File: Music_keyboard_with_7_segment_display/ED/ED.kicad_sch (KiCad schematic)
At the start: 1 part

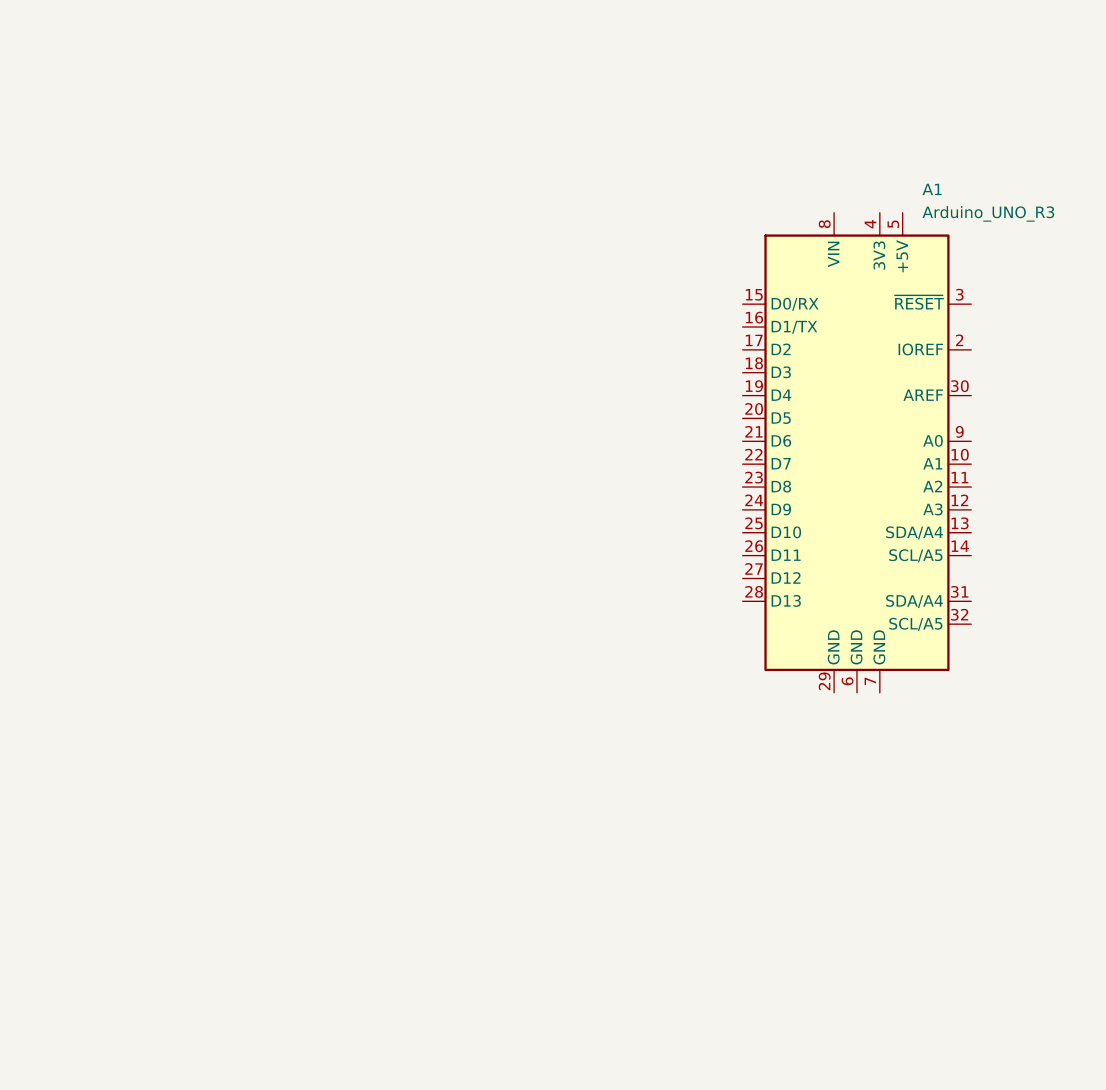
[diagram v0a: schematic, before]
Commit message: ED definition
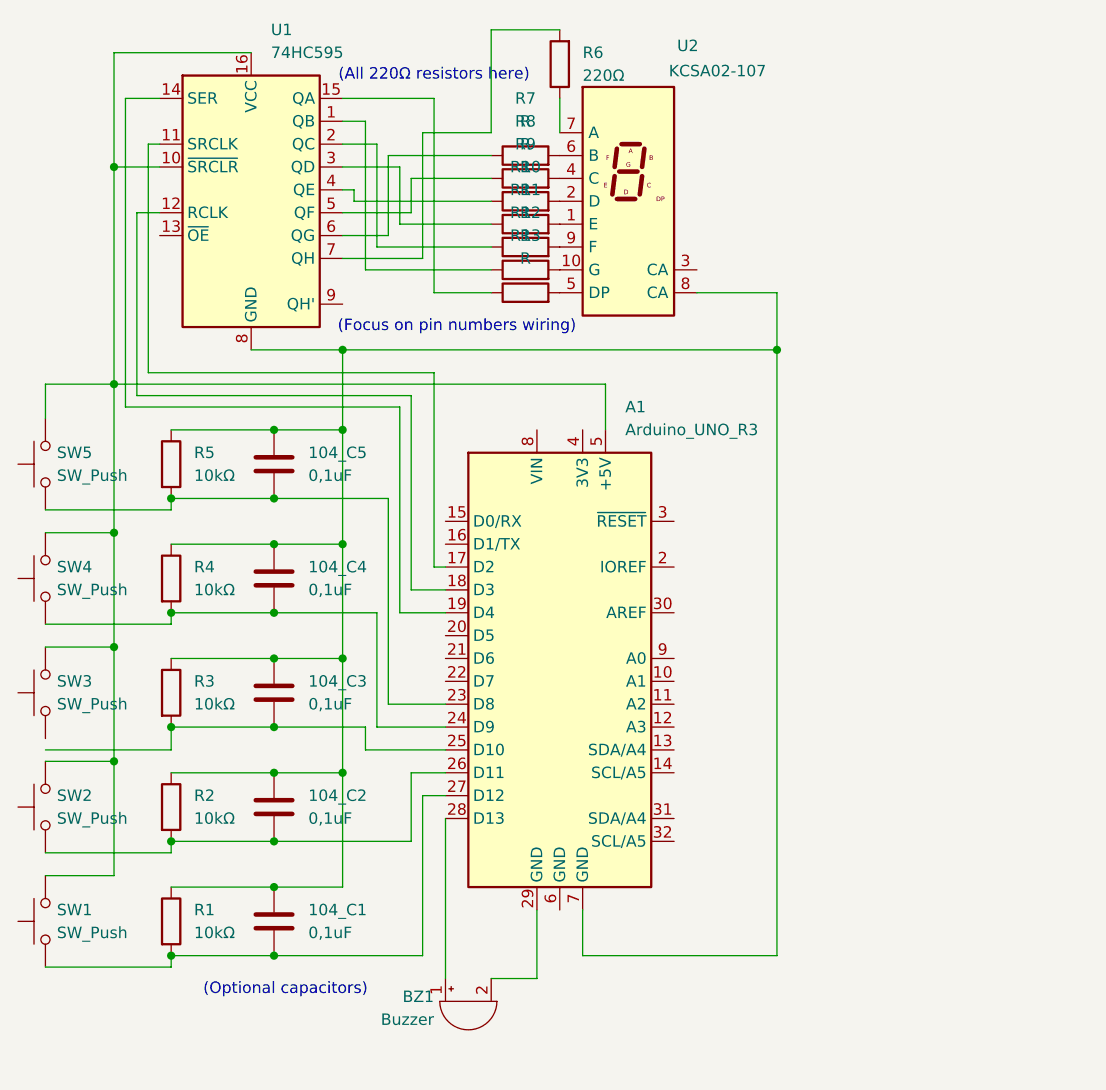
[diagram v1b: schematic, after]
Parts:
- added 104_C1, 104_C2, 104_C3, 104_C4, 104_C5: 0,1uF, symbol Device:C
- added BZ1: Buzzer, symbol Device:Buzzer
- added R1, R2, R3, R4, R5: 10kΩ, symbol Device:R
- added R10, R11, R12, R13, R7, R8, R9: R, symbol Device:R
- added R6: 220Ω, symbol Device:R
- added SW1, SW2, SW3, SW4, SW5: SW_Push, symbol Switch:SW_Push
- added U1: 74HC595, symbol 74xx:74HC595
- added U2: KCSA02-107, Display_7Segment:KCSC02-107, symbol Display_Character:KCSA02-107
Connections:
- net at A1.17 (D2): now also U1.11 (SRCLK)
- net at A1.18 (D3): now also U1.12 (RCLK)
- net at A1.19 (D4): now also U1.14 (SER)
- net at A1.23 (D8): now also 104_C5.2, R5.2, SW5.1
- net at A1.24 (D9): now also 104_C4.2, R4.2, SW4.1
- net at A1.25 (D10): now also 104_C3.2, R3.2
- net at A1.26 (D11): now also 104_C2.2, R2.2, SW2.1
- net at A1.27 (D12): now also 104_C1.2, R1.2, SW1.1
- net at A1.28 (D13): now also BZ1.1 (+)
- net at A1.29 (GND): now also BZ1.2 (-)
- net at A1.5 (+5V): now also SW1.2, SW2.2, SW3.2, SW4.2, SW5.2, U1.10 (~{SRCLR}), U1.16 (VCC)
- net at A1.7 (GND): now also 104_C1.1, 104_C2.1, 104_C3.1, 104_C4.1, 104_C5.1, R1.1, R2.1, R3.1, R4.1, R5.1, U1.8 (GND), U2.8 (CA)
- new net: R10.1, U1.3 (QD)
- new net: R10.2, U2.1 (E)
- new net: R8.1, U1.5 (QF)
- new net: R8.2, U2.4 (C)
- new net: R12.1, U1.1 (QB)
- new net: R13.1, U1.15 (QA)
- new net: R11.1, U1.2 (QC)
- new net: R9.1, U1.4 (QE)
- new net: R7.1, U1.6 (QG)
- new net: R6.2, U1.7 (QH)
- new net: R13.2, U2.5 (DP)
- new net: R12.2, U2.10 (G)
- new net: R9.2, U2.2 (D)
- new net: R7.2, U2.6 (B)
- new net: R6.1, U2.7 (A)
- new net: R11.2, U2.9 (F)
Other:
- note added: "(All 220Ω resistors here)"
- note added: "(Focus on pin numbers wiring)"
- note added: "(Optional capacitors)"
- moved on the sheet: A1

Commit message: GuitarNeck
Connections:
- net at 104_C3.2, A1.25 (D10), R3.2: now also SW3.1
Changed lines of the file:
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@@
 	(wire
 		(pts
-			(xy 104.14 118.11) (xy 118.11 118.11)
+			(xy 104.14 116.84) (xy 118.11 116.84)
 		)
 		(stroke
@@
 	(wire
 		(pts
-			(xy 118.11 115.57) (xy 118.11 118.11)
-		)
-		(stroke
+			(xy 118.11 115.57) (xy 118.11 116.84)
+		)
+		(stroke

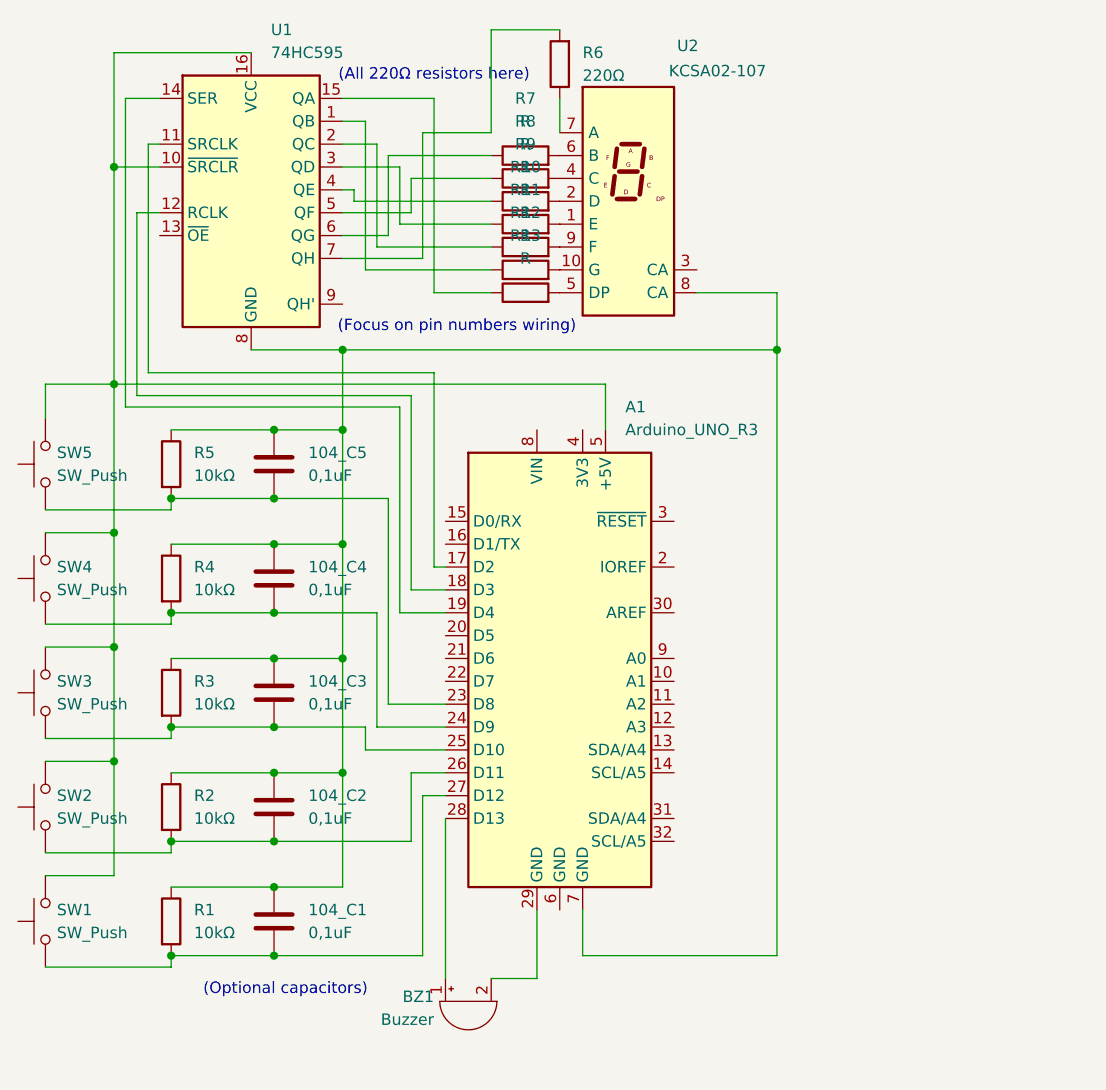
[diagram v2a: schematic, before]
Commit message: Capacitors before buttons and buzzer connected to pwm pin 6
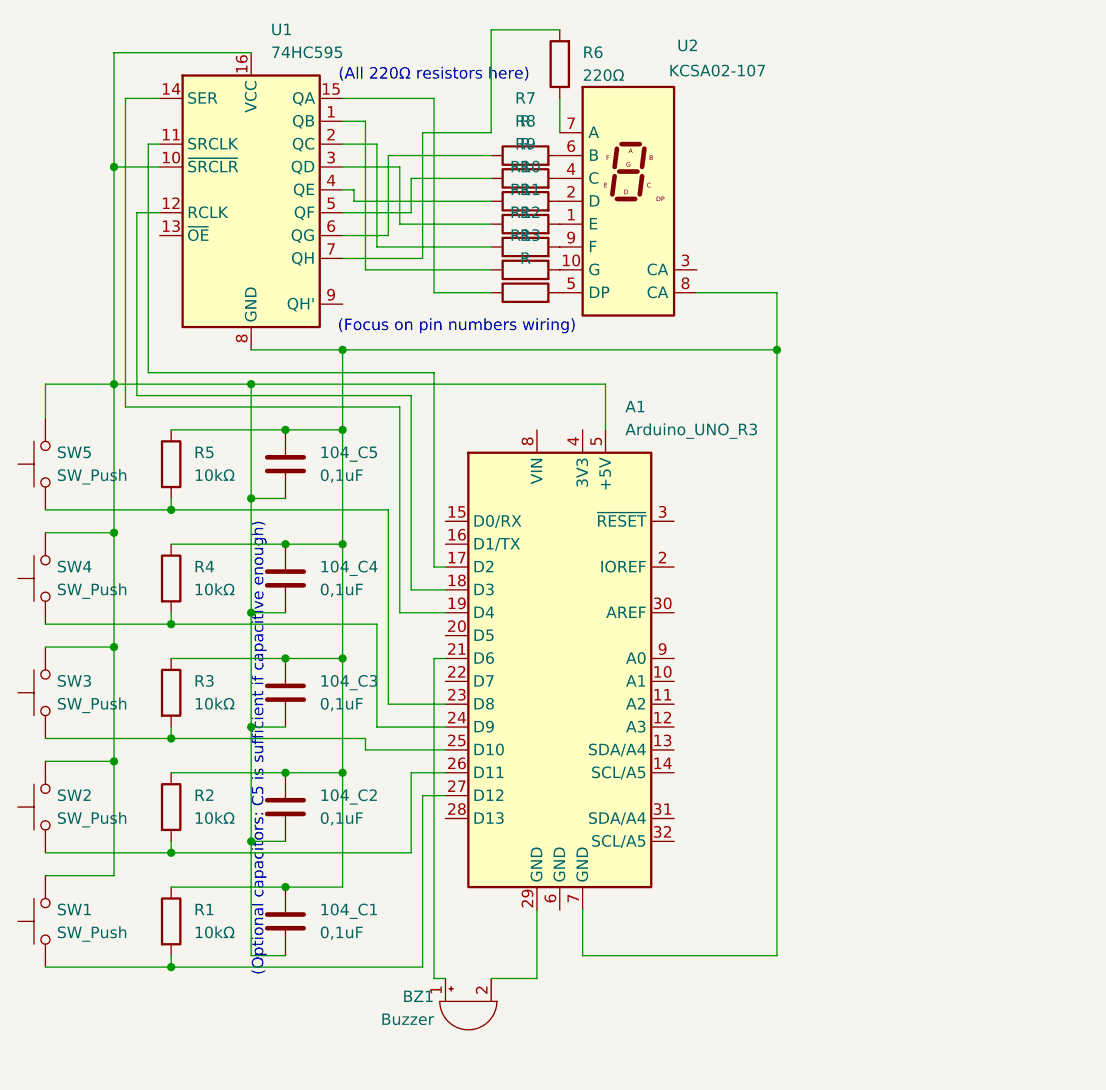
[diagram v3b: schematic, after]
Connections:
- net at A1.26 (D11), R2.2, SW2.1: no longer 104_C2.2
- net at A1.5 (+5V), SW1.2, SW2.2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: now also 104_C1.2, 104_C2.2, 104_C3.2, 104_C4.2, 104_C5.2
- net at A1.23 (D8), R5.2, SW5.1: no longer 104_C5.2
- net at A1.24 (D9), R4.2, SW4.1: no longer 104_C4.2
- net at A1.21 (D6): now also BZ1.1 (+)
- net at A1.25 (D10), R3.2, SW3.1: no longer 104_C3.2
- net at A1.27 (D12), R1.2, SW1.1: no longer 104_C1.2
- net at A1.28 (D13): no longer BZ1.1 (+)
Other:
- note added: "(Optional capacitors: C5 is sufficient if capacitive enough)"
- note removed: "(Optional capacitors)"
- moved on the sheet: 104_C1, 104_C2, 104_C3, 104_C4, 104_C5

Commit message: New note
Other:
- note added: "(Is R5 sufficient for all buttons?)"
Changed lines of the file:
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@@
 	(generator_version "9.0")
 	(paper "A4")
+	(text "(Is R5 sufficient for all buttons?)"
+		(exclude_from_sim no)
+		(at 115.062 116.586 90)
+		(effects
+			(font
+				(size 1.27 1.27)
+			)
+		)
+	)
 	(text "(Optional capacitors: C5 is sufficient if capacitive enough)"
 		(exclude_from_sim no)
